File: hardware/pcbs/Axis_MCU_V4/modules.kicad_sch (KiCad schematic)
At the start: 42 parts, among them U10 TXS0108E, U11 TXS0108E, U12 SN74LVC1G08, U13 SN74LVC1G08, U14 TXS0108E, U15 TXS0108E, U16 SN74LVC1G08, U17 SN74LVC1G08, U18 TXS0108E, U19 TXS0108E, U20 SN74LVC1G08, U21 SN74LVC1G08, U22 TXS0108E, U23 TXS0108E, U7 SN74LVC1G08, U8 SN74LVC1G08, U9 SN74HCS139PW

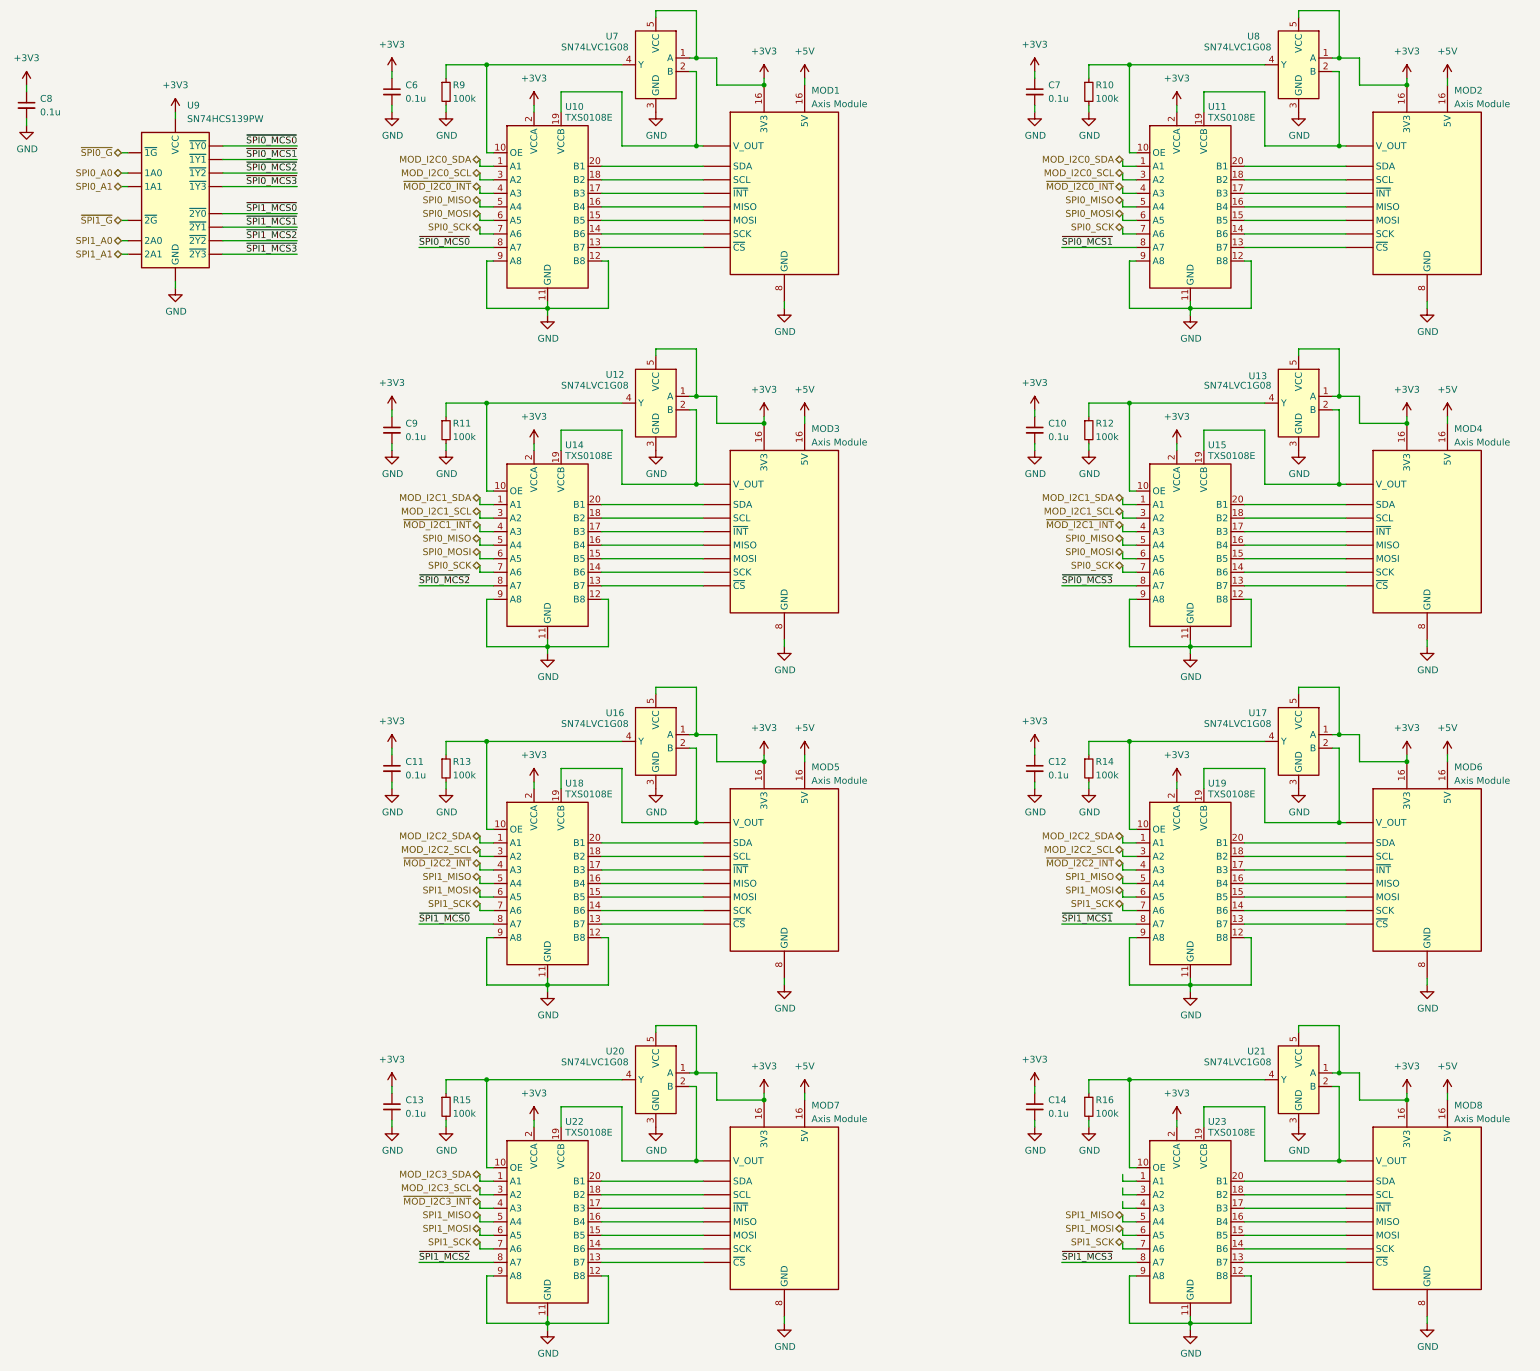
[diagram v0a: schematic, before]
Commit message: Add base board
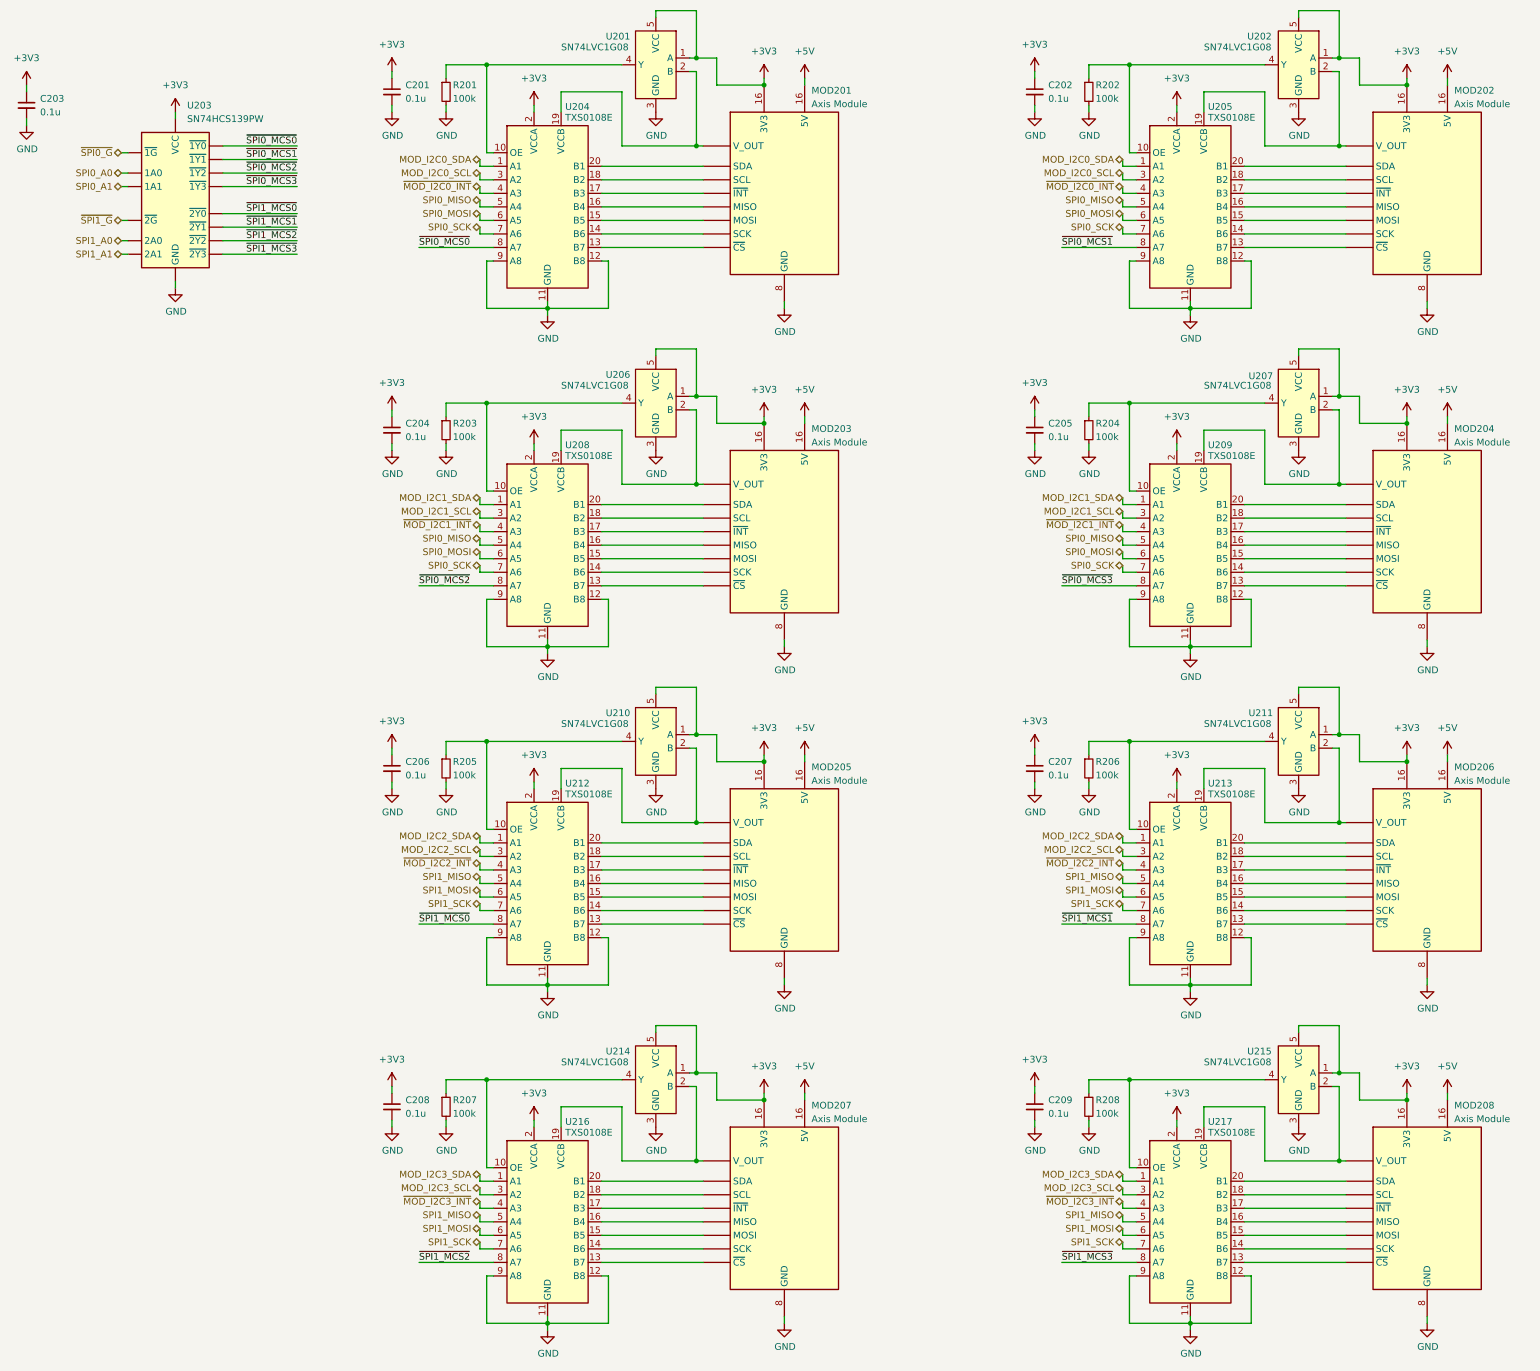
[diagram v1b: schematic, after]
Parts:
- renumbered C6 to C201, C7 to C202, C8 to C203, C9 to C204, C10 to C205, C11 to C206, C12 to C207, C13 to C208, C14 to C209, MOD1 to MOD201, MOD2 to MOD202, MOD3 to MOD203, MOD4 to MOD204, MOD5 to MOD205, MOD6 to MOD206, MOD7 to MOD207, MOD8 to MOD208, R9 to R201, R10 to R202, R11 to R203, R12 to R204, R13 to R205, R14 to R206, R15 to R207, R16 to R208, U7 to U201, U8 to U202, U9 to U203, U10 to U204, U11 to U205, U12 to U206, U13 to U207, U14 to U208, U15 to U209, U16 to U210, U17 to U211, U18 to U212, U19 to U213, U20 to U214, U21 to U215, U22 to U216, U23 to U217
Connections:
- net MOD_I2C3_SCL: now also U217.3 (A2)
- net MOD_I2C3_SDA: now also U217.1 (A1)
- net ~{MOD_I2C3_INT}: now also U217.4 (A3)
